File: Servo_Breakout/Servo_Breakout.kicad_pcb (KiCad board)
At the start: 4 copper layers, 96.5 x 31 mm, 32 parts, among them J101 395221002, J102 Conn_01x03, J103 Conn_01x04, Q101 2N7002, U101 TVS0500DRV, U301 STPS15H100CBY-TR, U302 BD9G500EFJ-LAE2, U401 TXS0102DCT

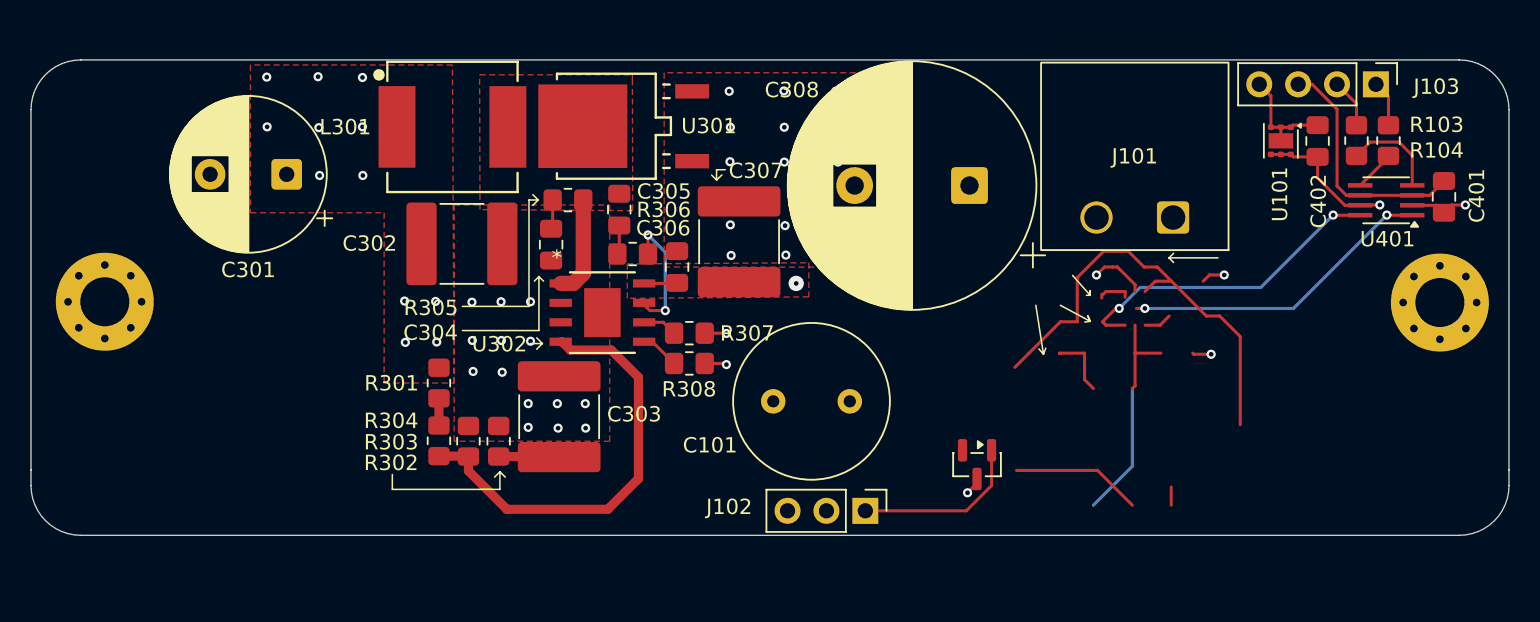
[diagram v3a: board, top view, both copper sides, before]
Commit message: completed layout rework for two 555 timers
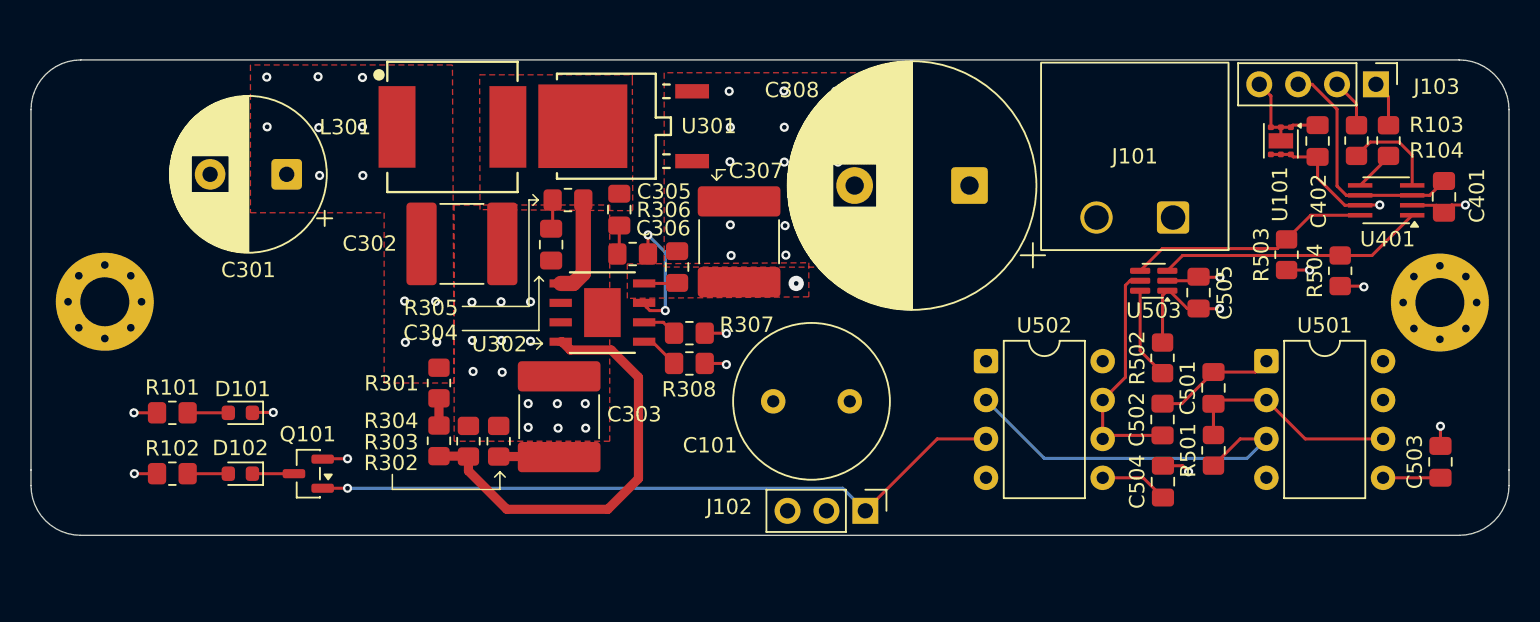
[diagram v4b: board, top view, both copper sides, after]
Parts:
- added C501: 0.1uF/X7R, Capacitor_SMD:C_0805_2012Metric_Pad1.18x1.45mm_HandSolder, F.Cu at (132.9, 72.4)
- added C502: C, Capacitor_SMD:C_0805_2012Metric_Pad1.18x1.45mm_HandSolder, F.Cu at (129.6, 74.5)
- added C503: 0.1uF/X7R, Capacitor_SMD:C_0805_2012Metric_Pad1.18x1.45mm_HandSolder, F.Cu at (147.7, 77.2)
- added C504: 0.1uF/X7R, Capacitor_SMD:C_0805_2012Metric_Pad1.18x1.45mm_HandSolder, F.Cu at (129.6, 78.5)
- added C505: 0.1uF, Capacitor_SMD:C_0805_2012Metric_Pad1.18x1.45mm_HandSolder, F.Cu at (131.9, 66.2)
- added D101: RED_LED, LED_SMD:LED_0603_1608Metric, F.Cu at (69.3, 74.0)
- added D102: GREEN_LED, LED_SMD:LED_0603_1608Metric, F.Cu at (69.3, 78.0)
- added R101: 470, Resistor_SMD:R_0805_2012Metric_Pad1.20x1.40mm_HandSolder, F.Cu at (64.9, 74.0)
- added R102: 470, Resistor_SMD:R_0805_2012Metric_Pad1.20x1.40mm_HandSolder, F.Cu at (64.9, 78.0)
- added R501: 142k, Resistor_SMD:R_0805_2012Metric_Pad1.20x1.40mm_HandSolder, F.Cu at (132.9, 76.5)
- added R502: 4.7k, Resistor_SMD:R_0805_2012Metric_Pad1.20x1.40mm_HandSolder, F.Cu at (129.6, 70.4)
- added R503: 4.7k, Resistor_SMD:R_0805_2012Metric_Pad1.20x1.40mm_HandSolder, F.Cu at (137.7, 63.7)
- added R504: 4.7k, Resistor_SMD:R_0805_2012Metric_Pad1.20x1.40mm_HandSolder, F.Cu at (141.2, 64.8)
- added U501: ICM7555xP, Package_DIP:DIP-8_W7.62mm, F.Cu at (136.4, 70.7)
- added U502: ICM7555xP, Package_DIP:DIP-8_W7.62mm, F.Cu at (118.0, 70.7)
- added U503: MCP4018-xxxxLT, Package_TO_SOT_SMD:SOT-363_SC-70-6, F.Cu at (129.0, 65.4)
- moved Q101 43.7 mm to (73.8, 78.0), turned to 180 degrees
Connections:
- Q101 pad 2: /LED_GREEN -> GND
- Q101 pad 3: /VBUCK -> /LED_GREEN
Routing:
- net /PWM_A1: track 11.2 -> 45.9 mm, vias 0 -> 1
- net /Timer/VCC: track 30.8 -> 0.00 mm
- net /Timer/TIM1_OUT: track 0.00 -> 24.6 mm
- net Net-(U502-DISCH): track 0.00 -> 15.7 mm
- net Net-(D502-K): track 14.6 -> 0.00 mm
- net Net-(U501-THRES): track 0.00 -> 14.3 mm
- net /VBUCK: track 10.5 -> 22.8 mm, vias 14 -> 18
- net GND: track 24.2 -> 35.2 mm, vias 35 -> 37
- net Net-(U501-OUT): track 8.51 -> 0.00 mm
- net Net-(U503-A): track 0.00 -> 5.99 mm
- net /I2C1_SDA: track 21.3 -> 15.9 mm, vias 2 -> 0
- net /I2C1_SCL: track 22.7 -> 17.5 mm, vias 2 -> 0
- net Net-(U502-CONT): track 0.00 -> 4.47 mm
- net Net-(D502-A): track 4.21 -> 0.00 mm
- net Net-(U501-CONT): track 0.00 -> 3.75 mm
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
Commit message: servo board final cleanup
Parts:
- removed R103, R104: 1k, Resistor_SMD:R_0805_2012Metric_Pad1.20x1.40mm_HandSolder
- added C406: 0.1uF/X7R, Capacitor_SMD:C_0805_2012Metric_Pad1.18x1.45mm_HandSolder, F.Cu at (114.4, 79.0)
- added R205: 0, Resistor_SMD:R_0805_2012Metric_Pad1.20x1.40mm_HandSolder, F.Cu at (88.2, 74.1)
- added U404: SN74LVC2G14DBV, Package_TO_SOT_SMD:SOT-23-6, F.Cu at (114.2, 75.8)
- C203: renamed from C303; value 15uF/100V -> 6800pF/50V; footprint Capacitor_SMD:C_2220_5750Metric_Pad1.97x5.40mm_HandSolder -> Capacitor_SMD:C_0805_2012Metric_Pad1.18x1.45mm_HandSolder
- C404: renamed from C502; value C -> 0.1uF
- J102: renamed from J103; footprint Connector_PinHeader_2.54mm:PinHeader_1x04_P2.54mm_Vertical -> Connector_PinHeader_2.54mm:PinHeader_1x05_P2.54mm_Vertical
- moved J102 2.59 mm to (146.1, 52.6)
- moved C203 1.42 mm to (90.2, 75.7)
- renumbered C301 to C201, C302 to C202, C304 to C204, C305 to C205, C306 to C206, C307 to C207, C308 to C208, C401 to C301, C402 to C302, C503 to C401, C501 to C402, C505 to C403, C504 to C405, J102 to J103, L301 to L201, R301 to R201, R302 to R202, R303 to R203, R304 to R204, R305 to R206, R306 to R207, R307 to R208, R308 to R209, R501 to R401, R503 to R402, R504 to R403, R502 to R404, U301 to U201, U302 to U202, U401 to U301, U501 to U401, U503 to U402, U502 to U403
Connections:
- C203 pad 2: GND -> Net-(U202-COMP)
- J102 pad 1: Net-(J103-Pin_1) -> /SW_EN
- J102 pad 2: Net-(J103-Pin_2) -> /CONN_I2C1_SCL
- J102 pad 3: /I2C1_VCC -> /CONN_I2C1_SDA
- J102 pad 4: GND -> /I2C1_VCC
- U202 pad 3: GND -> Net-(U202-COMP)
- U403 pad 3: /PWM_A1 -> Net-(U403-OUT)
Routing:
- net /SW_EN: track 2.25 -> 57.6 mm, vias 0 -> 1
- net Net-(U202-COMP): track 0.00 -> 10.4 mm
- net Net-(U202-FB): track 28.5 -> 20.7 mm
- net /VBUCK: track 22.8 -> 28.3 mm
- net /PWM_A1: track 45.9 -> 40.8 mm
- net /CONN_I2C1_SDA: track 2.69 -> 7.23 mm
- net /Timer/INV_OUT: track 0.00 -> 3.48 mm
- net Net-(U403-OUT): track 0.00 -> 3.34 mm
- net Net-(J103-Pin_2): track 3.20 -> 0.00 mm
- net Net-(J103-Pin_1): track 3.01 -> 0.00 mm
- net GND: track 35.2 -> 36.7 mm
- net /CONN_I2C1_SCL: track 6.34 -> 7.58 mm

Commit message: servo breakout gerbers
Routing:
- net +36V: vias 1 -> 3
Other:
- board text added: "Servo Breakout Noah B Thomas M"
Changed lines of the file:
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@@
 	)
 	(paper "A4")
+	(title_block
+		(title "Servo Breakout")
+		(date "2026-03-24")
+		(rev "A")
+		(company "University of Illinois Urbana-Champaign")
+		(comment 4 "Contributors: Noah Breit, Thomas McManamen")
+	)
 	(layers
 		(0 "F.Cu" signal)
@@
 			(plot_on_all_layers_selection 0x00000000_00000000_00000000_00000000)
 			(disableapertmacros no)
-			(usegerberextensions no)
+			(usegerberextensions yes)
 			(usegerberattributes yes)
 			(usegerberadvancedattributes yes)
-			(creategerberjobfile yes)
+			(creategerberjobfile no)
 			(dashed_line_dash_ratio 12.000000)
 			(dashed_line_gap_ratio 3.000000)
@@
 			(sketchdnponfab yes)
 			(crossoutdnponfab yes)
-			(subtractmaskfromsilk no)
+			(subtractmaskfromsilk yes)
 			(outputformat 1)
 			(mirror no)
-			(drillshape 1)
+			(drillshape 0)
 			(scaleselection 1)
-			(outputdirectory "")
+			(outputdirectory "gerbers/")
 		)
 	)
@@
 		(layer "User.1")
 	)
+	(gr_text "Servo Breakout\nNoah B\nThomas M"
+		(at 65 66.8 0)
+		(layer "B.SilkS")
+		(effects
+			(font
+				(size 2 2)
+				(thickness 0.3)
+			)
+			(justify right mirror)
+		)
+	)
 	(segment
 		(start 139.7 55.2375)
@@
 		(at 105.65 65.575)
 		(size 1)
-		(drill 0.3)
+		(drill 0.5)
+		(layers "F.Cu" "B.Cu")
+		(free yes)
+		(net 4)
+	)
+	(via
+		(at 106.7 65.6)
+		(size 1)
+		(drill 0.5)
+		(layers "F.Cu" "B.Cu")
+		(free yes)
+		(net 4)
+	)
+	(via
+		(at 107.7 65.6)
+		(size 1)
+		(drill 0.5)
 		(layers "F.Cu" "B.Cu")
 		(free yes)
@@
 		(polygon
 			(pts
-				(xy 94.62 64.3) (xy 106.475 64.225) (xy 106.475 66.45) (xy 94.62 66.55)
+				(xy 94.62 64.3) (xy 108.275 64.213612) (xy 108.275 66.434816) (xy 94.62 66.55)
 			)
 		)
